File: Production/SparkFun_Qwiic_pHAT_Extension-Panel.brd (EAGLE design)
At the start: 65 x 78.4 mm, 77 parts, among them J1 RASPBERRYPI-40-PIN-GPIO_SMD_M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, J2 RASPBERRYPI-40-PIN-GPIO_RIGHT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, J3 QWIIC_RIGHT_ANGLE, J5 QWIIC_RIGHT_ANGLE

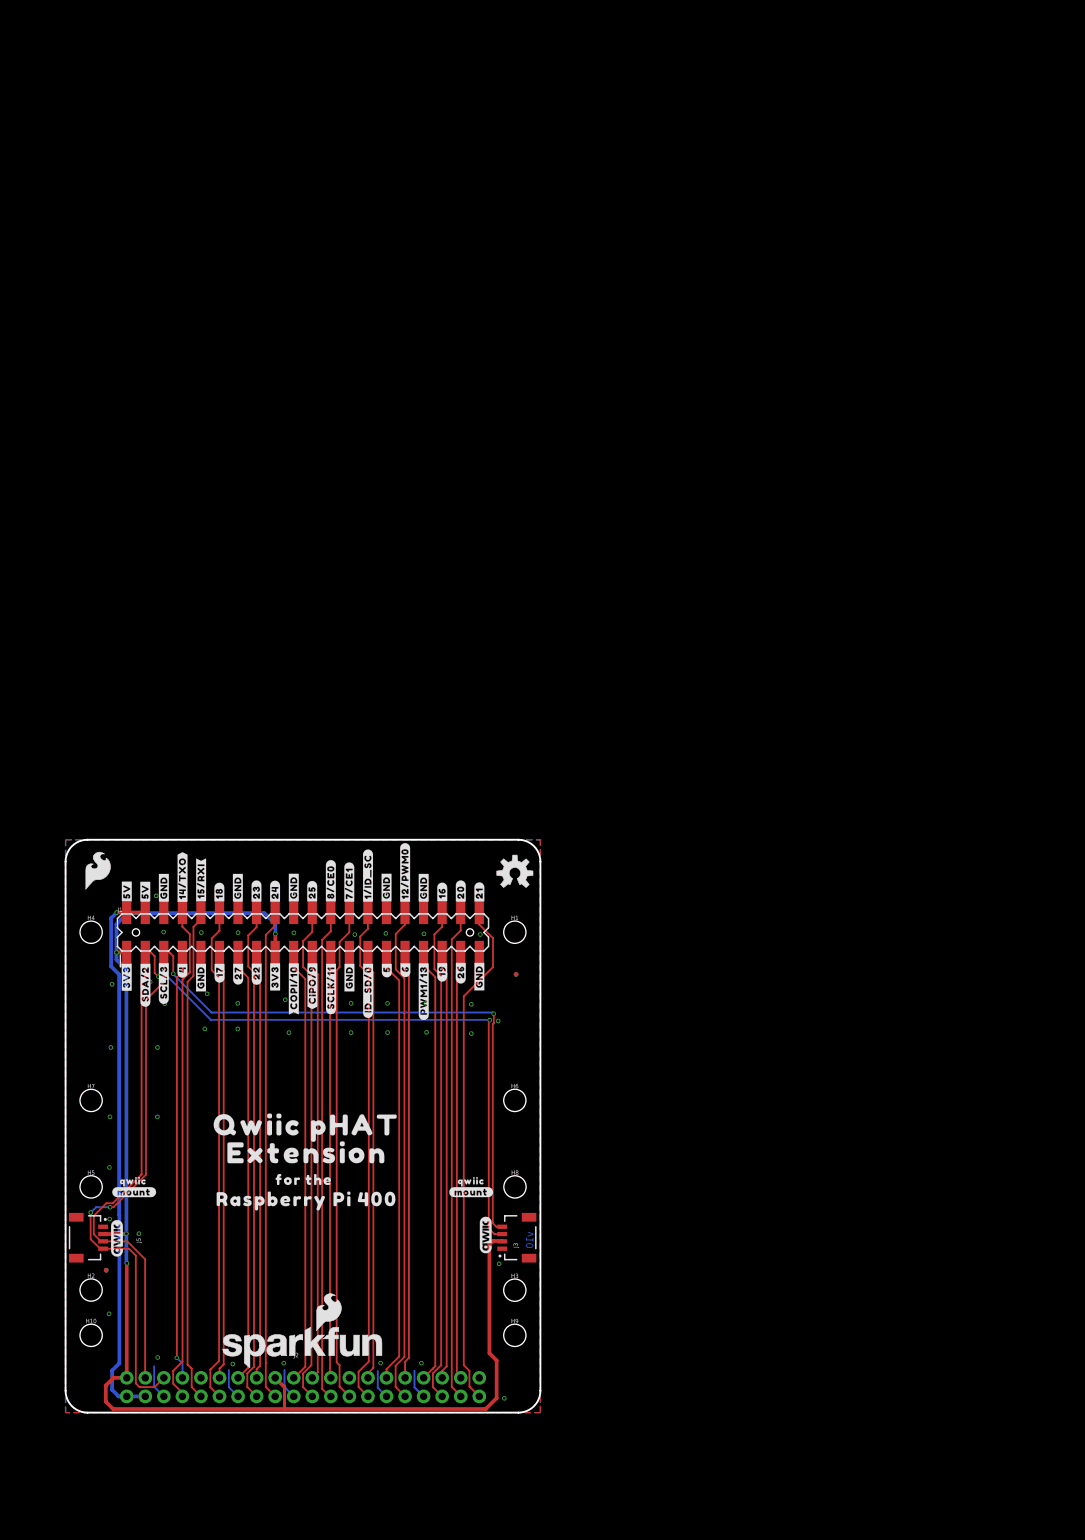
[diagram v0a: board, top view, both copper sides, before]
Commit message: Adds 2x2 production panel
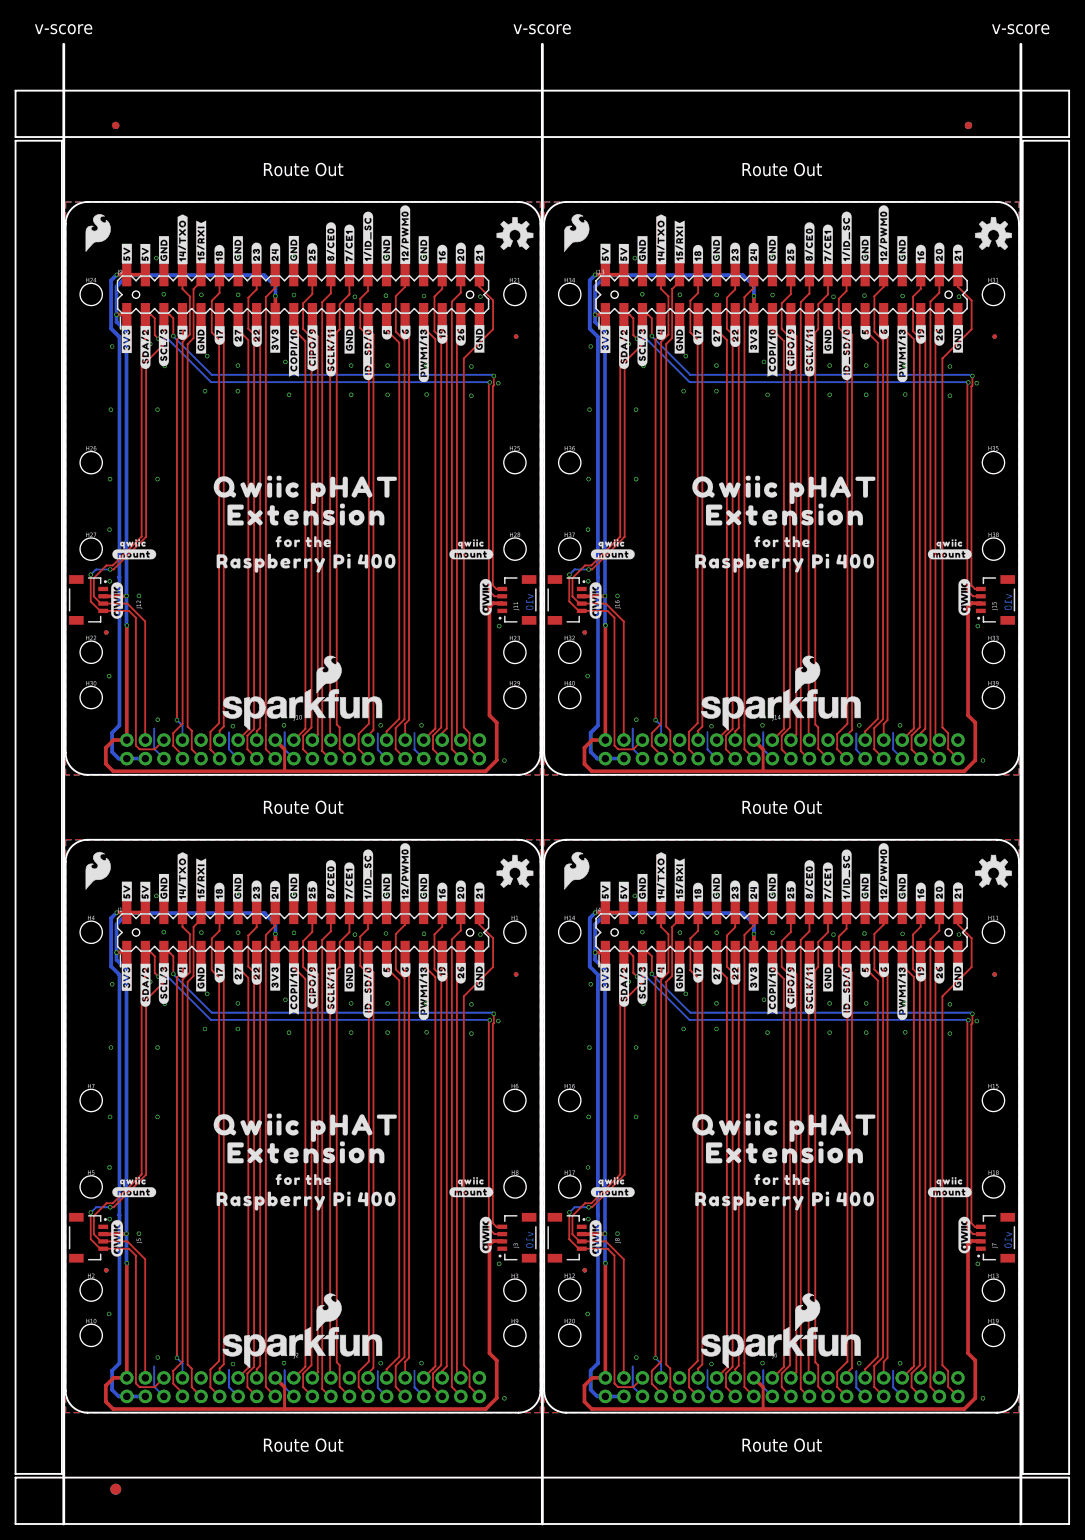
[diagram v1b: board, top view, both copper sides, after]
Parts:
- removed FRAME1: FRAME-LETTER, SparkFun-Aesthetics:CREATIVE_COMMONS
- added E$1, E$2, E$3, E$4: (no value), SparkFun-Aesthetics:FIDUCIAL-1X2
- added E$5, E$6: (no value), SparkFun-Retired:FIDUCIAL-1.5X3
- added FD10, FD11, FD12, FD13, FD14, FD15, FD16, FD5, FD6, FD7, FD8, FD9: FIDUCIALUFIDUCIAL, SparkFun-Aesthetics:FIDUCIAL-MICRO
- added H11, H12, H13, H14, H15, H16, H17, H18, H19, H20, H21, H22, H23, H24, H25, H26, H27, H28, H29, H30, H31, H32, H33, H34, H35, H36, H37, H38, H39, H40: STAND-OFFTIGHT, SparkFun-Hardware:STAND-OFF-TIGHT
- added J10, J14, J6: RASPBERRYPI-40-PIN-GPIO_RIGHT_ANGLE, SparkFun-Connectors:2X20_RIGHT_ANGLE
- added J11, J12, J15, J16, J7, J8: QWIIC_RIGHT_ANGLE, SparkFun-Connectors:JST04_1MM_RA
- added J13, J4, J9: RASPBERRYPI-40-PIN-GPIO_SMD_MALE, SparkFun-Connectors:RASPBERRY_PI_HAT_40_PIN_SMD_MALE
- added LOGO10, LOGO12, LOGO15, LOGO17, LOGO20, LOGO7: SFE_LOGO_NAME_FLAME.2_INCH, SparkFun-Aesthetics:SFE_LOGO_NAME_FLAME_.2
- added LOGO11, LOGO14, LOGO16, LOGO19, LOGO6, LOGO9: QWIIC_LOGO_5MM, SparkFun-Aesthetics:QWIIC_5MM
- added LOGO13, LOGO18, LOGO8: OSHW-LOGOM, SparkFun-Aesthetics:OSHW-LOGO-M
- added U$100, U$103, U$153, U$156, U$206, U$209: (no value), top:EXTENSION32
- added U$101, U$104, U$154, U$157, U$207, U$210: (no value), top:RASPBERRY_PI_40033
- added U$102, U$152, U$155, U$205, U$208, U$99: (no value), top:QWIIC_PHAT31
- added U$105, U$106, U$158, U$159, U$211, U$212: (no value), top:FOR_THE40034
- added U$107, U$108, U$160, U$161, U$41, U$42: (no value), top:#3V3#0
- added U$109, U$162, U$43: (no value), top:#4#4
- added U$110, U$163, U$44: (no value), top:#5#28
- added U$111, U$112, U$164, U$165, U$45, U$46: (no value), top:#5V#28
- added U$113, U$166, U$47: (no value), top:#6#28
- added U$114, U$167, U$48: (no value), top:#7#CE1#29
- added U$115, U$168, U$49: (no value), top:#8#CE0#29
- added U$116, U$169, U$50: (no value), top:#12#PWM0#29
- added U$117, U$170, U$53: (no value), top:#16#29
- added U$118, U$171, U$54: (no value), top:#17#5
- added U$119, U$172, U$55: (no value), top:#18#29
- added U$120, U$173, U$56: (no value), top:#19#28
- added U$121, U$174, U$57: (no value), top:#20#29
- added U$122, U$175, U$58: (no value), top:#21#29
- added U$123, U$176, U$59: (no value), top:#22#28
- added U$124, U$177, U$60: (no value), top:#23#29
- added U$125, U$178, U$61: (no value), top:#24#29
- added U$126, U$179, U$62: (no value), top:#25#29
- added U$127, U$180, U$63: (no value), top:#26#28
- added U$128, U$181, U$64: (no value), top:#27#18
- added U$129, U$130, U$131, U$132, U$133, U$134, U$135, U$136, U$182, U$183, U$184, U$185, U$186, U$187, U$188, U$189, U$65, U$66, U$67, U$68, U$69, U$70, U$71, U$72: (no value), top:#GND#28
- added U$137, U$190, U$73: (no value), top:#1#ID_SC#29
- added U$138, U$191, U$74: (no value), top:#SDA#2#4
- added U$139, U$192, U$77: (no value), top:#SCL#3#4
- added U$140, U$193, U$78: (no value), top:#SCLK#11#28
- added U$141, U$194, U$79: (no value), top:#ID_SD#0#28
- added U$142, U$195, U$80: (no value), top:#PWM1#13#28
- added U$143, U$196, U$87: (no value), SparkFun-Aesthetics:SFE_LOGO_FLAME_.2
- added U$144, U$197, U$88: (no value), top:#CIPO#9#28
- added U$145, U$198, U$92: (no value), top:#COPI#10#28
- added U$146, U$147, U$199, U$200, U$93, U$94: (no value), top:#MOUNT#29
- added U$148, U$149, U$201, U$202, U$95, U$96: (no value), top:QWIIC30
- added U$150, U$203, U$97: (no value), top:#14#TXO#29
- added U$151, U$204, U$98: (no value), top:#15#RXI#29
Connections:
- new net 0/ID_SD1: J4.27, J6.27
- new net 0/ID_SD2: J10.27, J9.27
- new net 0/ID_SD3: J13.27, J14.27
- new net 1/ID_SC1: J4.28, J6.28
- new net 1/ID_SC2: J10.28, J9.28
- new net 1/ID_SC3: J13.28, J14.28
- new net 10/COPI1: J4.19, J6.19
- new net 10/COPI2: J10.19, J9.19
- new net 10/COPI3: J13.19, J14.19
- new net 11/SCLK1: J4.23, J6.23
- new net 11/SCLK2: J10.23, J9.23
- new net 11/SCLK3: J13.23, J14.23
- new net 12/PWM1: J4.32, J6.32
- new net 12/PWM2: J10.32, J9.32
- new net 12/PWM3: J13.32, J14.32
- new net 13/PWM2: J4.33, J6.33
- new net 13/PWM3: J10.33, J9.33
- new net 13/PWM4: J13.33, J14.33
- new net 14/TXO1: J4.8, J6.8
- new net 14/TXO2: J10.8, J9.8
- new net 14/TXO3: J13.8, J14.8
- new net 15/RXI1: J4.10, J6.10
- new net 15/RXI2: J10.10, J9.10
- new net 15/RXI3: J13.10, J14.10
- new net 18/PCM_CLK1: J4.12, J6.12
- new net 18/PCM_CLK2: J10.12, J9.12
- new net 18/PCM_CLK3: J13.12, J14.12
- new net 19/PCM_FS1: J4.35, J6.35
- new net 19/PCM_FS2: J10.35, J9.35
- new net 19/PCM_FS3: J13.35, J14.35
- new net 2/SDA1: J4.3, J6.3, J7.3, J8.3
- new net 2/SDA2: J10.3, J11.3, J12.3, J9.3
- new net 2/SDA3: J13.3, J14.3, J15.3, J16.3
- new net 20/PCM_DIN1: J4.38, J6.38
- new net 20/PCM_DIN2: J10.38, J9.38
- new net 20/PCM_DIN3: J13.38, J14.38
- new net 21/PCM_DOUT1: J4.40, J6.40
- new net 21/PCM_DOUT2: J10.40, J9.40
- new net 21/PCM_DOUT3: J13.40, J14.40
- new net 3.3V1: J4.1, J4.17, J6.1, J6.17, J7.2, J8.2
- new net 3.3V2: J10.1, J10.17, J11.2, J12.2, J9.1, J9.17
- new net 3.3V3: J13.1, J13.17, J14.1, J14.17, J15.2, J16.2
- new net 3/SCL1: J4.5, J6.5, J7.4, J8.4
- new net 3/SCL2: J10.5, J11.4, J12.4, J9.5
- new net 3/SCL3: J13.5, J14.5, J15.4, J16.4
- new net 5V1: J4.2, J4.4, J6.2, J6.4
- new net 5V2: J10.2, J10.4, J9.2, J9.4
- new net 5V3: J13.2, J13.4, J14.2, J14.4
- new net 7/CE2: J4.26, J6.26
- new net 7/CE3: J10.26, J9.26
- new net 7/CE4: J13.26, J14.26
- new net 8/CE1: J4.24, J6.24
- new net 8/CE2: J10.24, J9.24
- new net 8/CE3: J13.24, J14.24
- new net 9/CIPO1: J4.21, J6.21
- new net 9/CIPO2: J10.21, J9.21
- new net 9/CIPO3: J13.21, J14.21
- new net GND1: J4.14, J4.20, J4.25, J4.30, J4.34, J4.39, J4.6, J4.9, J6.14, J6.20, J6.25, J6.30, J6.34, J6.39, J6.6, J6.9, J7.1, J8.1
- new net GND2: J10.14, J10.20, J10.25, J10.30, J10.34, J10.39, J10.6, J10.9, J11.1, J12.1, J9.14, J9.20, J9.25, J9.30, J9.34, J9.39, J9.6, J9.9
- new net GND3: J13.14, J13.20, J13.25, J13.30, J13.34, J13.39, J13.6, J13.9, J14.14, J14.20, J14.25, J14.30, J14.34, J14.39, J14.6, J14.9, J15.1, J16.1
- new net GP1: J4.7, J6.7
- new net GP10: J4.16, J6.16
- new net GP11: J4.18, J6.18
- new net GP12: J4.22, J6.22
- new net GP13: J4.37, J6.37
- new net GP14: J4.13, J6.13
- new net GP15: J10.7, J9.7
- new net GP18: J10.29, J9.29
- new net GP19: J10.31, J9.31
- new net GP2: J4.29, J6.29
- new net GP20: J10.36, J9.36
- new net GP21: J10.11, J9.11
- new net GP28: J10.15, J9.15
- new net GP29: J10.16, J9.16
- new net GP3: J4.31, J6.31
- new net GP30: J10.18, J9.18
- new net GP31: J10.22, J9.22
- new net GP32: J10.37, J9.37
- new net GP33: J10.13, J9.13
- new net GP34: J13.7, J14.7
- new net GP35: J13.29, J14.29
- new net GP36: J13.31, J14.31
- new net GP37: J13.36, J14.36
- new net GP38: J13.11, J14.11
- new net GP39: J13.15, J14.15
- new net GP40: J13.16, J14.16
- new net GP41: J13.18, J14.18
- new net GP42: J13.22, J14.22
- new net GP43: J13.37, J14.37
- new net GP44: J13.13, J14.13
- new net GP7: J4.36, J6.36
- new net GP8: J4.11, J6.11
- new net GP9: J4.15, J6.15
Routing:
- net 3.3V1: track 0.00 -> 182.4 mm, vias 0 -> 4
- net 3.3V2: track 0.00 -> 182.4 mm, vias 0 -> 4
- net 3.3V3: track 0.00 -> 182.4 mm, vias 0 -> 4
- net 3/SCL1: track 0.00 -> 154.3 mm, vias 0 -> 4
- net 3/SCL3: track 0.00 -> 154.3 mm, vias 0 -> 4
- net 3/SCL2: track 0.00 -> 154.3 mm, vias 0 -> 4
- net 2/SDA3: track 0.00 -> 149.8 mm, vias 0 -> 2
- net 2/SDA2: track 0.00 -> 149.8 mm, vias 0 -> 2
- net 2/SDA1: track 0.00 -> 149.8 mm, vias 0 -> 2
- net 5V3: track 0.00 -> 75.4 mm, vias 0 -> 1
- net 5V2: track 0.00 -> 75.4 mm, vias 0 -> 1
- net 5V1: track 0.00 -> 75.4 mm, vias 0 -> 1
- net 21/PCM_DOUT2: track 0.00 -> 69.6 mm
- net 21/PCM_DOUT1: track 0.00 -> 69.6 mm
- net 21/PCM_DOUT3: track 0.00 -> 69.6 mm
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- added copper zone on layer 1, net GND1
- added copper zone on layer 16, net GND1
- added copper zone on layer 1, net GND2
- added copper zone on layer 16, net GND2
- added copper zone on layer 1, net GND3
- added copper zone on layer 16, net GND3
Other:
- board size 65 x 78.4 mm -> 144.2 x 202.6 mm
- board text added: "Route Out"
- board text added: "v-score"
- board text removed: "Elias Santistevan"

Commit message: Moves fiducials on the panel to the attached portions of the panel frame
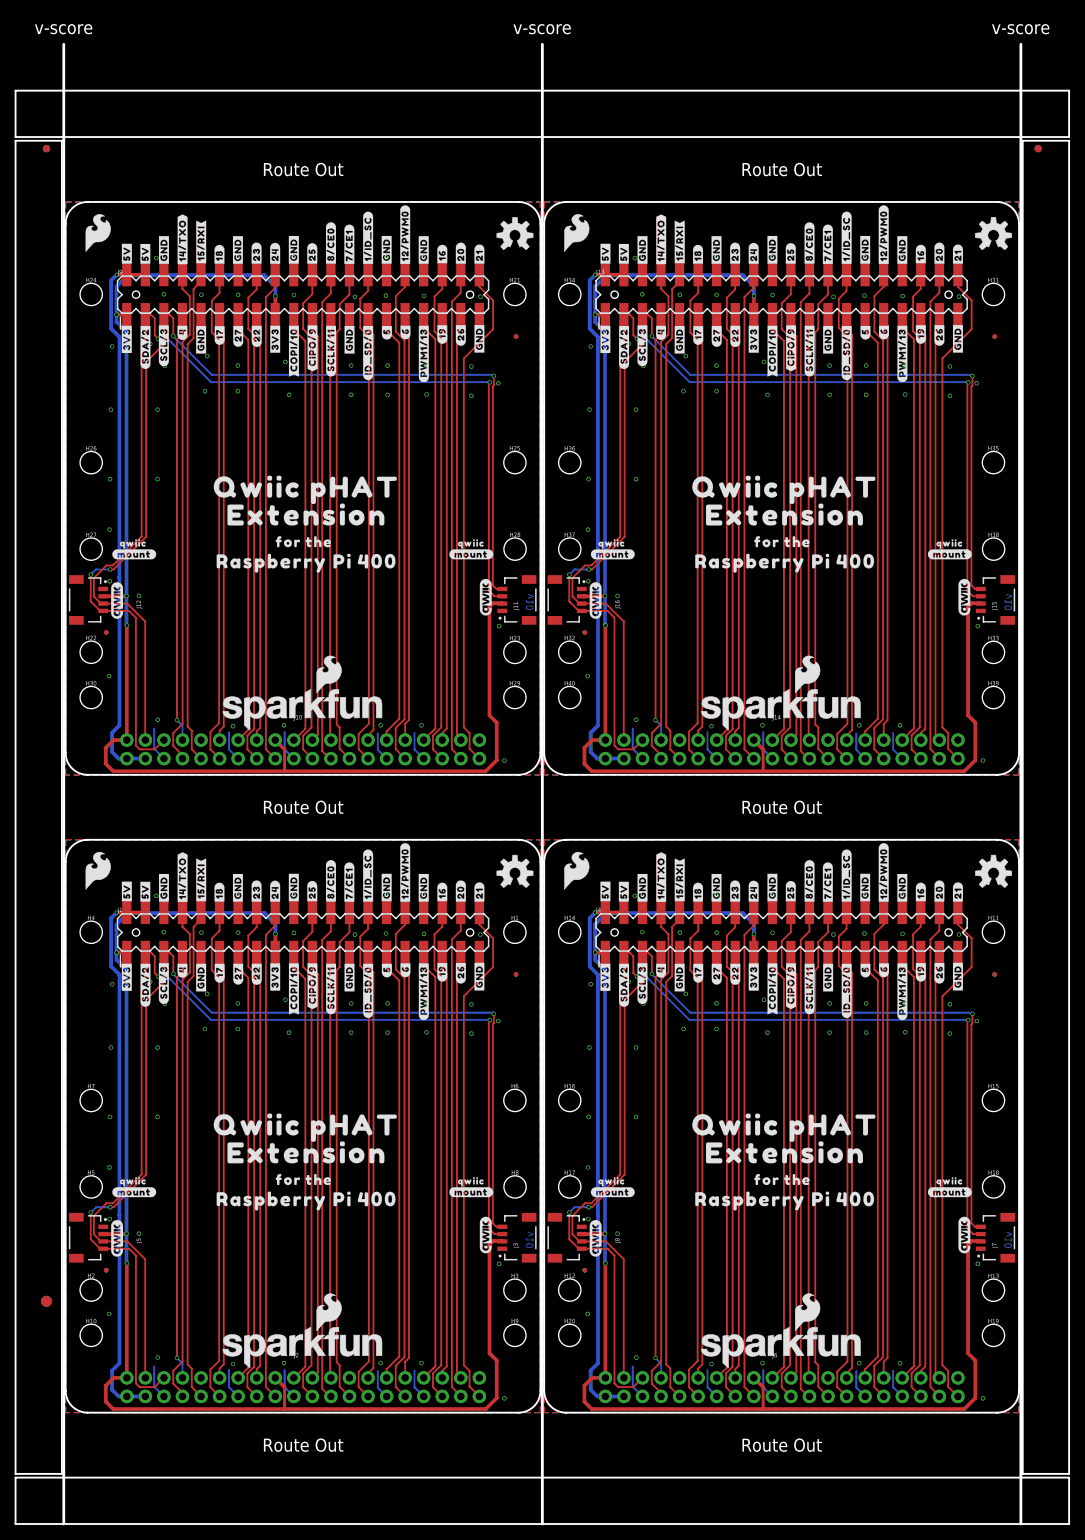
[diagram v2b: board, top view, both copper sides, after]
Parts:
- moved E$5 27.4 mm to (-2.62, 15.2)
- moved E$6 27.4 mm to (-2.62, 15.2)
- moved E$3 10.1 mm to (133.1, 173.0)
- moved E$4 10.1 mm to (133.1, 173.0)
- moved E$1 10.00 mm to (-2.62, 173.0)
- moved E$2 10.00 mm to (-2.62, 173.0)
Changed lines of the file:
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@@
 <attribute name="VALUE" x="69.0093" y="96.237878125" size="0.6096" layer="27" font="vector" ratio="20" align="top-center"/>
 </element>
-<element name="E$1" library="SparkFun-Aesthetics" package="FIDUCIAL-1X2" value="" x="6.858" y="176.20488125" smashed="yes"/>
-<element name="E$2" library="SparkFun-Aesthetics" package="FIDUCIAL-1X2" value="" x="6.858" y="176.20488125" smashed="yes" rot="MR0"/>
-<element name="E$3" library="SparkFun-Aesthetics" package="FIDUCIAL-1X2" value="" x="123.586240625" y="176.20488125" smashed="yes"/>
-<element name="E$4" library="SparkFun-Aesthetics" package="FIDUCIAL-1X2" value="" x="123.586240625" y="176.20488125" smashed="yes" rot="MR0"/>
-<element name="E$5" library="SparkFun-Retired" package="FIDUCIAL-1.5X3" value="" x="6.858" y="-10.4775" smashed="yes"/>
-<element name="E$6" library="SparkFun-Retired" package="FIDUCIAL-1.5X3" value="" x="6.858" y="-10.4775" smashed="yes" rot="MR0"/>
+<element name="E$1" library="SparkFun-Aesthetics" package="FIDUCIAL-1X2" value="" x="-2.62381875" y="173.02988125" smashed="yes"/>
+<element name="E$2" library="SparkFun-Aesthetics" package="FIDUCIAL-1X2" value="" x="-2.62381875" y="173.02988125" smashed="yes" rot="MR0"/>
+<element name="E$3" library="SparkFun-Aesthetics" package="FIDUCIAL-1X2" value="" x="133.131559375" y="173.02988125" smashed="yes"/>
+<element name="E$4" library="SparkFun-Aesthetics" package="FIDUCIAL-1X2" value="" x="133.131559375" y="173.02988125" smashed="yes" rot="MR0"/>
+<element name="E$5" library="SparkFun-Retired" package="FIDUCIAL-1.5X3" value="" x="-2.62381875" y="15.24" smashed="yes"/>
+<element name="E$6" library="SparkFun-Retired" package="FIDUCIAL-1.5X3" value="" x="-2.62381875" y="15.24" smashed="yes" rot="MR0"/>
 </elements>
 <signals>
